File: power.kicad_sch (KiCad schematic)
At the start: 85 parts, among them Q10 2NPN, Q3 PMOS, Q4 PMOS, Q5 PMOS, Q6 PMOS, Q7 2NPN, Q9 2PNP, U21 TPS62410, U22 LDO-2V5, U28 AP22652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

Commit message: Reduce antenna bias current limit to 125 mA
Change all 162k resistors to 180k
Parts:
- R46, R47: value 162k -> 180k±1%; Part Number RC0402FR-07162KL -> RC0402FR-07180KL
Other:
- note removed: "1%"
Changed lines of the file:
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@@
 		)
 	)
-	(text "1%"
-		(exclude_from_sim no)
-		(at 124.46 24.13 0)
-		(effects
-			(font
-				(size 1.016 1.016)
-			)
-			(justify left bottom)
-		)
-	)
 	(text "Power Input"
 		(exclude_from_sim no)
@@
 		)
 	)
-	(text "1%"
-		(exclude_from_sim no)
-		(at 147.32 24.13 0)
-		(effects
-			(font
-				(size 1.016 1.016)
-			)
-			(justify left bottom)
-		)
-	)
 	(label "VBUS"
 		(at 46.99 185.42 90)
@@
 			)
 		)
-		(property "Value" "162k"
+		(property "Value" "180k±1%"
 			(at 148.59 21.59 90)
 			(effects
@@
 			)
 		)
-		(property "Description" "RES 1/16W 162K OHM 1% 0402"
+		(property "Description" "RES 180K OHM 1% 1/16W 0402"
 			(at 148.59 25.4 0)
 			(effects
@@
 			)
 		)
-		(property "Part Number" "RC0402FR-07162KL"
+		(property "Part Number" "RC0402FR-07180KL"
 			(at 148.59 25.4 0)
 			(effects
@@
 		(fields_autoplaced yes)
 		(property "Reference" "R46"
-			(at 125.73 29.21 90)
+			(at 125.73 19.05 90)
 			(effects
 				(font
@@
 			)
 		)
-		(property "Value" "162k"
-			(at 125.73 31.75 90)
+		(property "Value" "180k±1%"
+			(at 125.73 21.59 90)
 			(effects
 				(font
@@
 			)
 		)
-		(property "Description" "RES 1/16W 162K OHM 1% 0402"
+		(property "Description" "RES 180K OHM 1% 1/16W 0402"
 			(at 125.73 25.4 0)
 			(effects
@@
 			)
 		)
-		(property "Part Number" "RC0402FR-07162KL"
+		(property "Part Number" "RC0402FR-07180KL"
 			(at 125.73 25.4 0)
 			(effects

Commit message: Update to KiCad 9
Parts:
- Q3, Q4, Q5, Q6: symbol Device:Q_PMOS_GSD -> Transistor_FET:Q_PMOS_GSD
- Q9: symbol Device:Q_Dual_PNP_PNP_E1B1C2E2B2C1 -> Transistor_BJT:Q_Dual_PNP_PNP_E1B1C2E2B2C1
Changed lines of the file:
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@@
 (kicad_sch
-	(version 20231120)
+	(version 20250114)
 	(generator "eeschema")
-	(generator_version "8.0")
+	(generator_version "9.0")
 	(paper "A4")
 	(title_block
@@
 		(comment 1 "${LICENSE}")
 	)
+	(text "current limit: 235 mA ±20%"
+		(exclude_from_sim no)
+		(at 101.6 172.72 0)
+		(effects
+			(font
+				(size 1.524 1.524)
+			)
+		)
+	)
+	(text "overvoltage shut-off\nthreshold: 5.5-6.0 V"
+		(exclude_from_sim no)
+		(at 107.95 97.79 0)
+		(effects
+			(font
+				(size 1.27 1.27)
+			)
+			(justify right bottom)
+		)
+	)
+	(text "Power Input"
+		(exclude_from_sim no)
+		(at 41.91 26.035 0)
+		(effects
+			(font
+				(size 3.4036 3.4036)
+			)
+			(justify left bottom)
+		)
+	)
+	(text "The MCU can disable either power input.\nOvervoltage protection cannot be disabled."
+		(exclude_from_sim no)
+		(at 73.66 120.65 0)
+		(effects
+			(font
+				(size 1.27 1.27)
+			)
+			(justify right bottom)
+		)
+	)
 	(junction
 		(at 68.58 91.44)
@@
 		)
 	)
-	(text "current limit: 235 mA ±20%"
-		(exclude_from_sim no)
-		(at 101.6 172.72 0)
-		(effects
-			(font
-				(size 1.524 1.524)
-			)
-		)
-	)
-	(text "overvoltage shut-off\nthreshold: 5.5-6.0 V"
-		(exclude_from_sim no)
-		(at 107.95 97.79 0)
-		(effects
-			(font
-				(size 1.27 1.27)
-			)
-			(justify right bottom)
-		)
-	)
-	(text "Power Input"
-		(exclude_from_sim no)
-		(at 41.91 26.035 0)
-		(effects
-			(font
-				(size 3.4036 3.4036)
-			)
-			(justify left bottom)
-		)
-	)
-	(text "The MCU can disable either power input.\nOvervoltage protection cannot be disabled."
-		(exclude_from_sim no)
-		(at 73.66 120.65 0)
-		(effects
-			(font
-				(size 1.27 1.27)
-			)
-			(justify right bottom)
-		)
-	)
 	(label "VBUS"
 		(at 46.99 185.42 90)
@@
 	)
 	(symbol
-		(lib_id "Device:Q_PMOS_GSD")
+		(lib_id "Transistor_FET:Q_PMOS_GSD")
 		(at 78.74 78.74 270)
 		(mirror x)
@@
 	)
 	(symbol
-		(lib_id "Device:Q_PMOS_GSD")
+		(lib_id "Transistor_FET:Q_PMOS_GSD")
 		(at 224.79 132.08 270)
 		(mirror x)
@@
 	)
 	(symbol
-		(lib_id "Device:Q_Dual_PNP_PNP_E1B1C2E2B2C1")
+		(lib_id "Transistor_BJT:Q_Dual_PNP_PNP_E1B1C2E2B2C1")
 		(at 57.15 43.18 0)
 		(mirror x)
@@
 	)
 	(symbol
-		(lib_id "Device:Q_PMOS_GSD")
+		(lib_id "Transistor_FET:Q_PMOS_GSD")
 		(at 78.74 36.83 270)
 		(mirror x)
@@
 	)
 	(symbol
-		(lib_id "Device:Q_Dual_PNP_PNP_E1B1C2E2B2C1")
+		(lib_id "Transistor_BJT:Q_Dual_PNP_PNP_E1B1C2E2B2C1")
 		(at 57.15 85.09 0)
 		(mirror x)
@@
 	)
 	(symbol
-		(lib_id "Device:Q_PMOS_GSD")
+		(lib_id "Transistor_FET:Q_PMOS_GSD")
 		(at 231.14 35.56 270)
 		(mirror x)

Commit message: Change RX RF amplifier to BFR840
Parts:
- R22, R57, R81, R83, R86, R87: footprint Resistor_SMD:R_0402_1005Metric -> Resistor_SMD:R_0201_0603Metric; Manufacturer Panasonic -> Yageo; Part Number ERJ-2GEJ333X -> RC0201JR-0733KL
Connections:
- net +5V: now also FB1.1; no longer FB1.2
- net at C143.1, D11.1 (K), D12.1 (K)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: now also FB1.2; no longer FB1.1
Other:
- moved on the sheet: FB1
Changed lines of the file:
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@@
 	(symbol
 		(lib_id "Device:FerriteBead")
-		(at 106.68 50.8 90)
-		(mirror x)
+		(at 106.68 50.8 270)
 		(unit 1)
 		(exclude_from_sim no)
@@
 		(on_board yes)
 		(dnp no)
-		(fields_autoplaced yes)
 		(property "Reference" "FB1"
-			(at 106.6292 43.18 90)
+			(at 106.7308 43.18 90)
 			(effects
 				(font
@@
 		)
 		(property "Value" "Ferrite"
-			(at 106.6292 45.72 90)
+			(at 106.7308 45.72 90)
 			(effects
 				(font
@@
 			)
 		)
-		(property "Footprint" "Resistor_SMD:R_0402_1005Metric"
+		(property "Footprint" "Resistor_SMD:R_0201_0603Metric"
 			(at 76.962 96.52 90)
 			(effects
@@
 			)
 		)
-		(property "Description" "RES SMD 33K OHM 5% 1/10W 0402"
+		(property "Description" "RES 33K OHM 5% 1/20W 0201"
 			(at 78.74 96.52 0)
 			(effects
@@
 			)
 		)
-		(property "Manufacturer" "Panasonic"
+		(property "Manufacturer" "Yageo"
 			(at 78.74 96.52 0)
 			(effects
@@
 			)
 		)
-		(property "Part Number" "ERJ-2GEJ333X"
+		(property "Part Number" "RC0201JR-0733KL"
 			(at 78.74 96.52 0)
 			(effects
@@
 			)
 		)
-		(property "Footprint" "Resistor_SMD:R_0402_1005Metric"
+		(property "Footprint" "Resistor_SMD:R_0201_0603Metric"
 			(at 76.962 52.07 90)
 			(effects
@@
 			)
 		)
-		(property "Description" "RES SMD 33K OHM 5% 1/10W 0402"
+		(property "Description" "RES 33K OHM 5% 1/20W 0201"
 			(at 78.74 52.07 0)
 			(effects
@@
 			)
 		)
-		(property "Manufacturer" "Panasonic"
+		(property "Manufacturer" "Yageo"
 			(at 78.74 52.07 0)
 			(effects
@@
 			)
 		)
-		(property "Part Number" "ERJ-2GEJ333X"
+		(property "Part Number" "RC0201JR-0733KL"
 			(at 78.74 52.07 0)
 			(effects
@@
 			)
 		)
-		(property "Footprint" "Resistor_SMD:R_0402_1005Metric"
+		(property "Footprint" "Resistor_SMD:R_0201_0603Metric"
 			(at 40.132 88.9 90)
 			(effects
@@
 			)
 		)
-		(property "Description" "RES SMD 33K OHM 5% 1/10W 0402"
+		(property "Description" "RES 33K OHM 5% 1/20W 0201"
 			(at 41.91 88.9 0)
 			(effects
@@
 			)
 		)
-		(property "Manufacturer" "Panasonic"
+		(property "Manufacturer" "Yageo"
 			(at 41.91 88.9 0)
 			(effects
@@
 			)
 		)
-		(property "Part Number" "ERJ-2GEJ333X"
+		(property "Part Number" "RC0201JR-0733KL"
 			(at 41.91 88.9 0)
 			(effects
@@
 			)
 		)
-		(property "Footprint" "Resistor_SMD:R_0402_1005Metric"
+		(property "Footprint" "Resistor_SMD:R_0201_0603Metric"
 			(at 46.99 86.868 90)
 			(effects
@@
 			)
 		)
-		(property "Description" "RES SMD 33K OHM 5% 1/10W 0402"
+		(property "Description" "RES 33K OHM 5% 1/20W 0201"
 			(at 46.99 85.09 0)
 			(effects
@@
 			)
 		)
-		(property "Part Number" "ERJ-2GEJ333X"
+		(property "Part Number" "RC0201JR-0733KL"
 			(at 46.99 85.09 0)
 			(effects
@@
 			)
 		)
-		(property "Manufacturer" "Panasonic"
+		(property "Manufacturer" "Yageo"
 			(at 46.99 85.09 0)
 			(effects
@@
 			)
 		)
-		(property "Footprint" "Resistor_SMD:R_0402_1005Metric"
+		(property "Footprint" "Resistor_SMD:R_0201_0603Metric"
 			(at 40.132 46.99 90)
 			(effects
@@
 			)
 		)
-		(property "Description" "RES SMD 33K OHM 5% 1/10W 0402"
+		(property "Description" "RES 33K OHM 5% 1/20W 0201"
 			(at 41.91 46.99 0)
 			(effects
@@
 			)
 		)
-		(property "Manufacturer" "Panasonic"
+		(property "Manufacturer" "Yageo"
 			(at 41.91 46.99 0)
 			(effects
@@
 			)
 		)
-		(property "Part Number" "ERJ-2GEJ333X"
+		(property "Part Number" "RC0201JR-0733KL"
 			(at 41.91 46.99 0)
 			(effects
@@
 			)
 		)
-		(property "Footprint" "Resistor_SMD:R_0402_1005Metric"
+		(property "Footprint" "Resistor_SMD:R_0201_0603Metric"
 			(at 46.99 44.958 90)
 			(effects
@@
 			)
 		)
-		(property "Description" "RES SMD 33K OHM 5% 1/10W 0402"
+		(property "Description" "RES 33K OHM 5% 1/20W 0201"
 			(at 46.99 43.18 0)
 			(effects
@@
 			)
 		)
-		(property "Part Number" "ERJ-2GEJ333X"
+		(property "Part Number" "RC0201JR-0733KL"
 			(at 46.99 43.18 0)
 			(effects
@@
 			)
 		)
-		(property "Manufacturer" "Panasonic"
+		(property "Manufacturer" "Yageo"
 			(at 46.99 43.18 0)
 			(effects

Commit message: Change TX RF amplifier to BGB741
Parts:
- R88, R89, R90, R91: Manufacturer Panasonic -> Yageo; Part Number ERJ-2RKF1872X -> RC0402FR-0718K7L
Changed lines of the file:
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@@
 			)
 		)
-		(property "Description" "RES SMD 18.7K OHM 1% 1/10W 0402"
+		(property "Description" "RES 18.7K OHM 1% 1/16W 0402"
 			(at 31.75 39.37 0)
 			(effects
@@
 			)
 		)
-		(property "Manufacturer" "Panasonic"
+		(property "Manufacturer" "Yageo"
 			(at 31.75 39.37 0)
 			(effects
@@
 			)
 		)
-		(property "Part Number" "ERJ-2RKF1872X"
+		(property "Part Number" "RC0402FR-0718K7L"
 			(at 31.75 39.37 0)
 			(effects
@@
 			)
 		)
-		(property "Description" "RES SMD 18.7K OHM 1% 1/10W 0402"
+		(property "Description" "RES 18.7K OHM 1% 1/16W 0402"
 			(at 31.75 81.28 0)
 			(effects
@@
 			)
 		)
-		(property "Manufacturer" "Panasonic"
+		(property "Manufacturer" "Yageo"
 			(at 31.75 81.28 0)
 			(effects
@@
 			)
 		)
-		(property "Part Number" "ERJ-2RKF1872X"
+		(property "Part Number" "RC0402FR-0718K7L"
 			(at 31.75 81.28 0)
 			(effects
@@
 			)
 		)
-		(property "Description" "RES SMD 18.7K OHM 1% 1/10W 0402"
+		(property "Description" "RES 18.7K OHM 1% 1/16W 0402"
 			(at 31.75 58.42 0)
 			(effects
@@
 			)
 		)
-		(property "Manufacturer" "Panasonic"
+		(property "Manufacturer" "Yageo"
 			(at 31.75 58.42 0)
 			(effects
@@
 			)
 		)
-		(property "Part Number" "ERJ-2RKF1872X"
+		(property "Part Number" "RC0402FR-0718K7L"
 			(at 31.75 58.42 0)
 			(effects
@@
 			)
 		)
-		(property "Description" "RES SMD 18.7K OHM 1% 1/10W 0402"
+		(property "Description" "RES 18.7K OHM 1% 1/16W 0402"
 			(at 31.75 100.33 0)
 			(effects
@@
 			)
 		)
-		(property "Manufacturer" "Panasonic"
+		(property "Manufacturer" "Yageo"
 			(at 31.75 100.33 0)
 			(effects
@@
 			)
 		)
-		(property "Part Number" "ERJ-2RKF1872X"
+		(property "Part Number" "RC0402FR-0718K7L"
 			(at 31.75 100.33 0)
 			(effects

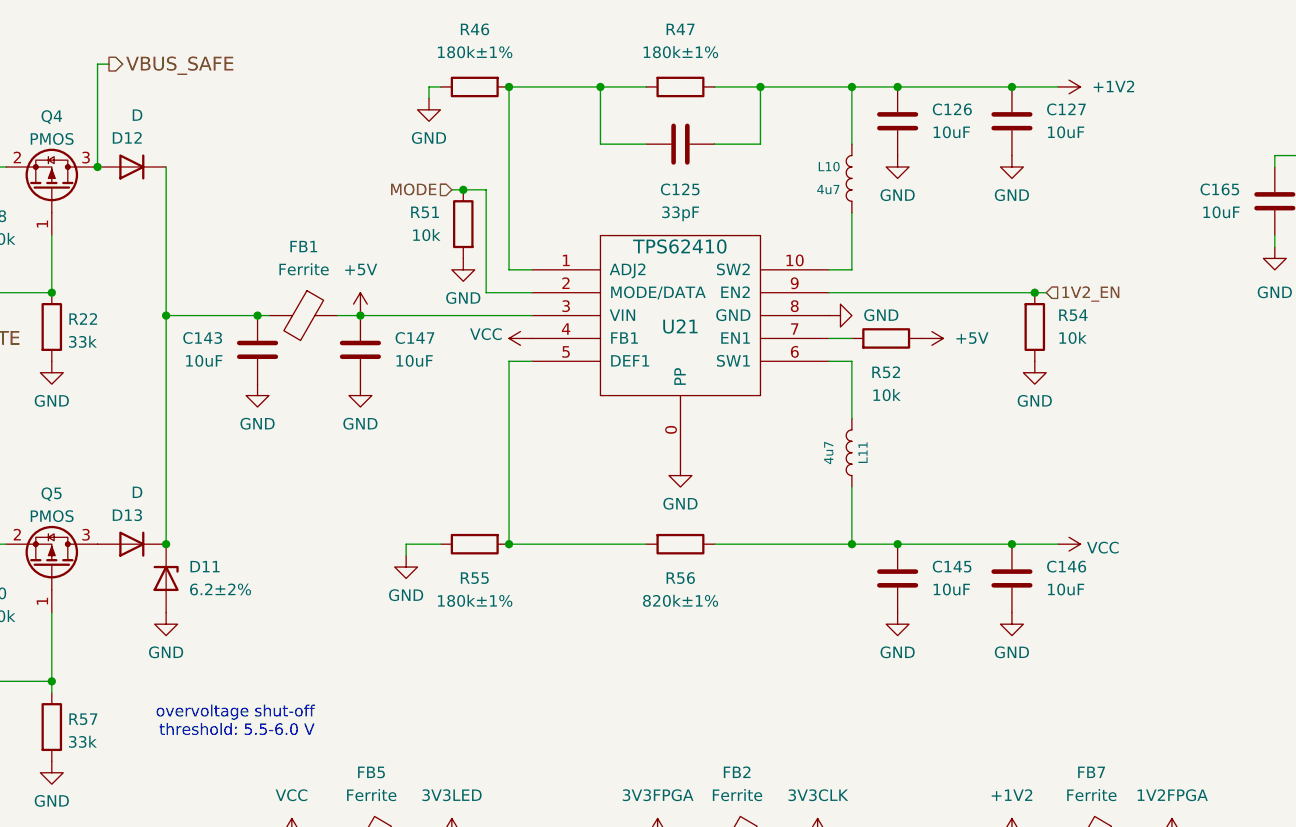
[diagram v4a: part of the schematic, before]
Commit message: Update symbols and footprints
- Update U21 symbol and footprint
- Add L10, L11 3D model
- Add T1, T2 3D model
- Update U29 footprint
- Update J10 footprint and part selection, change to TP6
- Update diode footprints and 3D models
- Update SMA connector footprint
- Fix 3D model scale for various footprints
- Change L1 from 0603 back to 0201
- Fix pin header 3D models
- Add component substitutions
- Update RF switch and amplifier footprints
- Remove fiducials
- Update mounting hole symbol and footprint
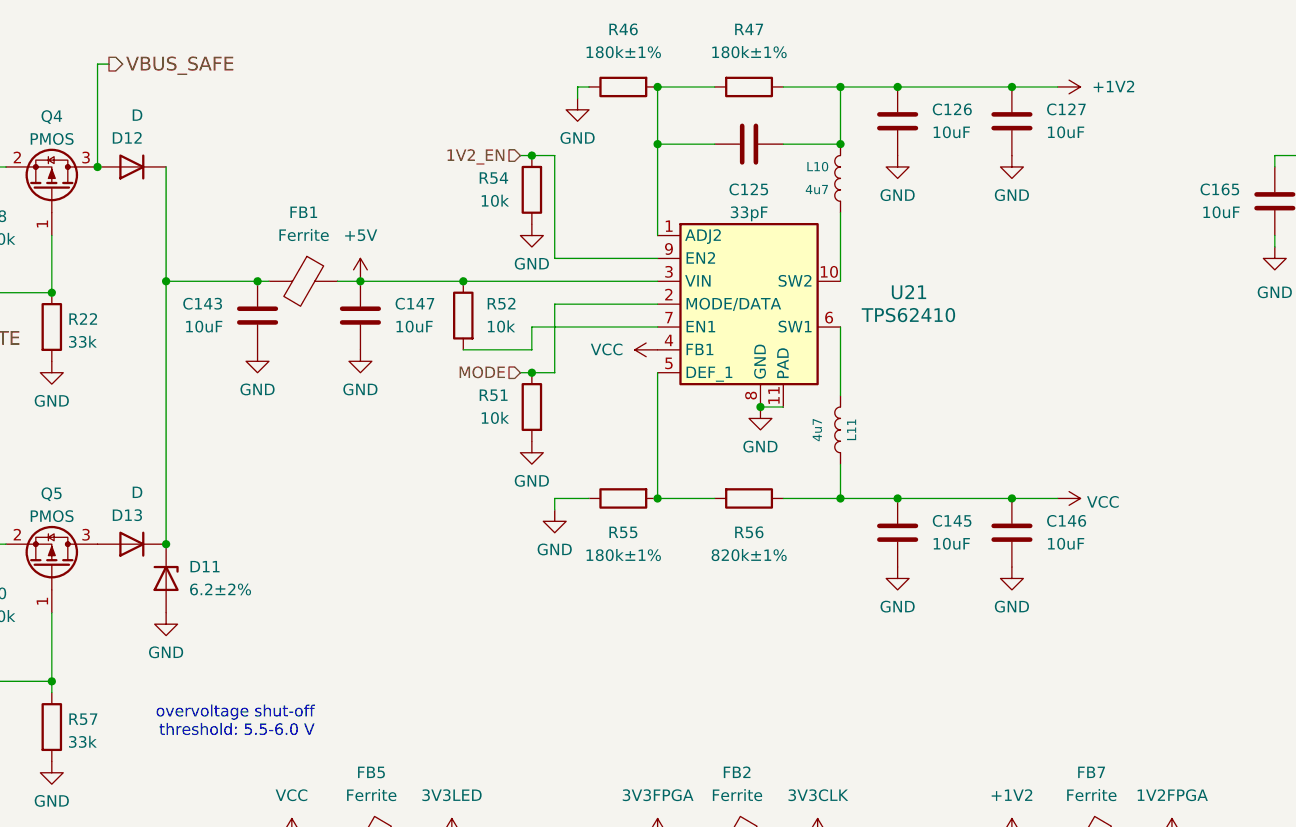
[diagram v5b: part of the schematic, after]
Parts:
- L11: Part Number NRS4018T4R7MDGJ -> LSXND4040TKL4R7MDG; Substitution NRG4026T4R7M -> NRS4018T4R7MDGJ, LLXND4040TKL4R7MDG, NRS4018T4R7MDGJ
- U21: footprint hackrf:GSG-S-PVSON-N10 -> praline:Texas_S-PVSON-N10_ThermalVias; symbol hackrf:TPS62410 -> praline:TPS62410
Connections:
- net GND: now also U21.11 (PAD); no longer U21.0 (PP)
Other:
- moved on the sheet: C125, C143, C145, C146, C147, FB1, L10, L11, R46, R47, R51, R52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

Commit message: Strengthen MODE and 1V2_EN pull-downs
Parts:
- R51, R54: value 10k -> 4k7; footprint Resistor_SMD:R_0402_1005Metric -> Resistor_SMD:R_0201_0603Metric; Part Number RC0402JR-0710KL -> RC0201FR-074K7L
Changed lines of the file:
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@@
 			)
 		)
-		(property "Value" "10k"
+		(property "Value" "4k7"
 			(at 129.54 38.0999 0)
 			(effects
@@
 			)
 		)
-		(property "Footprint" "Resistor_SMD:R_0402_1005Metric"
+		(property "Footprint" "Resistor_SMD:R_0201_0603Metric"
 			(at 132.08 36.83 0)
 			(effects
@@
 			)
 		)
-		(property "Description" "RES 10K OHM 1/16W 5% 0402 SMD"
+		(property "Description" "RES 4.7K OHM 1% 1/20W 0201"
 			(at 132.08 36.83 0)
 			(effects
@@
 			)
 		)
-		(property "Part Number" "RC0402JR-0710KL"
+		(property "Part Number" "RC0201FR-074K7L"
 			(at 132.08 36.83 0)
 			(effects
@@
 			)
 		)
-		(property "Value" "10k"
+		(property "Value" "4k7"
 			(at 129.54 62.2299 0)
 			(effects
@@
 			)
 		)
-		(property "Footprint" "Resistor_SMD:R_0402_1005Metric"
+		(property "Footprint" "Resistor_SMD:R_0201_0603Metric"
 			(at 132.08 60.96 0)
 			(effects
@@
 			)
 		)
-		(property "Description" "RES 10K OHM 1/16W 5% 0402 SMD"
+		(property "Description" "RES 4.7K OHM 1% 1/20W 0201"
 			(at 132.08 60.96 0)
 			(effects
@@
 			)
 		)
-		(property "Part Number" "RC0402JR-0710KL"
+		(property "Part Number" "RC0201FR-074K7L"
 			(at 132.08 60.96 0)
 			(effects

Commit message: Add M2 mounting holes
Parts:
- added TP6: TestPoint, TestPoint:TestPoint_Loop_D1.80mm_Drill1.0mm_Beaded, symbol Connector:TestPoint
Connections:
- net GND: now also TP6.1
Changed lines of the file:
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@@
+	)
+	(symbol
+		(lib_id "Connector:TestPoint")
+		(at 167.64 187.96 0)
+		(unit 1)
+		(exclude_from_sim no)
+		(in_bom yes)
+		(on_board yes)
+		(dnp yes)
+		(fields_autoplaced yes)
+		(property "Reference" "TP6"
+			(at 167.64 179.07 0)
+			(effects
+				(font
+					(size 1.016 1.016)
+				)
+			)
+		)
+		(property "Value" "TestPoint"
+			(at 167.64 181.61 0)
+			(effects
+				(font
+					(size 1.27 1.27)
+				)
+			)
+		)
+		(property "Footprint" "TestPoint:TestPoint_Loop_D1.80mm_Drill1.0mm_Beaded"
+			(at 167.64 187.96 0)
+			(effects
+				(font
+					(size 1.524 1.524)
+				)
+				(hide yes)
+			)
+		)
+		(property "Datasheet" "~"
+			(at 167.64 187.96 0)
+			(effects
+				(font
+					(size 1.524 1.524)
+				)
+				(hide yes)
+			)
+		)
+		(property "Description" ""
+			(at 167.64 187.96 0)
+			(effects
+				(font
+					(size 1.524 1.524)
+				)
+				(hide yes)
+			)
+		)
+		(property "Manufacturer" "Ronghe"
+			(at 167.64 187.96 0)
+			(effects
+				(font
+					(size 1.524 1.524)
+				)
+				(hide yes)
+			)
+		)
+		(property "Part Number" "RH-5001"
+			(at 167.64 187.96 0)
+			(effects
+				(font
+					(size 1.524 1.524)
+				)
+				(hide yes)
+			)
+		)
+		(pin "1"
+		)
+		(instances
+			(project "praline"
+				(path "/dba4afc6-760f-46cb-a936-032b76448f03/582bbebf-22b2-4cb5-8b91-2c73dca44d28"
+					(reference "TP6")
+					(unit 1)
+				)
+			)
+		)
+	)
+	(symbol
+		(lib_id "power:GND")
+		(at 167.64 187.96 0)
+		(unit 1)
+		(exclude_from_sim no)
+		(in_bom yes)
+		(on_board yes)
+		(dnp no)
+		(fields_autoplaced yes)
+		(property "Reference" "#PWR089"
+			(at 167.64 187.96 0)
+			(effects
+				(font
+					(size 0.762 0.762)
+				)
+				(hide yes)
+			)
+		)
+		(property "Value" "GND"
+			(at 167.64 189.738 0)
+			(effects
+				(font
+					(size 0.762 0.762)
+				)
+				(hide yes)
+			)
+		)
+		(property "Footprint" ""
+			(at 167.64 187.96 0)
+			(effects
+				(font
+					(size 1.524 1.524)
+				)
+			)
+		)
+		(property "Datasheet" ""
+			(at 167.64 187.96 0)
+			(effects
+				(font
+					(size 1.524 1.524)
+				)
+			)
+		)
+		(property "Description" "Power symbol creates a global label with name \"GND\" , ground"
+			(at 167.64 187.96 0)
+			(effects
+				(font
+					(size 1.27 1.27)
+				)
+				(hide yes)
+			)
+		)
+		(pin "1"
+		)
+		(instances
+			(project "praline"
+				(path "/dba4afc6-760f-46cb-a936-032b76448f03/582bbebf-22b2-4cb5-8b91-2c73dca44d28"
+					(reference "#PWR089")
+					(unit 1)
+				)
+			)
+		)
 	)
 	(symbol
